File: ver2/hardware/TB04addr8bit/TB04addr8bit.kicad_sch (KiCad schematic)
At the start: 15 parts, among them J1 USB_C_Receptacle_PowerOnly_6P, SW1 SW_SPDT, U1 74AHC04, U2 74AHC04, U3 74LS157, U4 74HC138, U5 74HC00

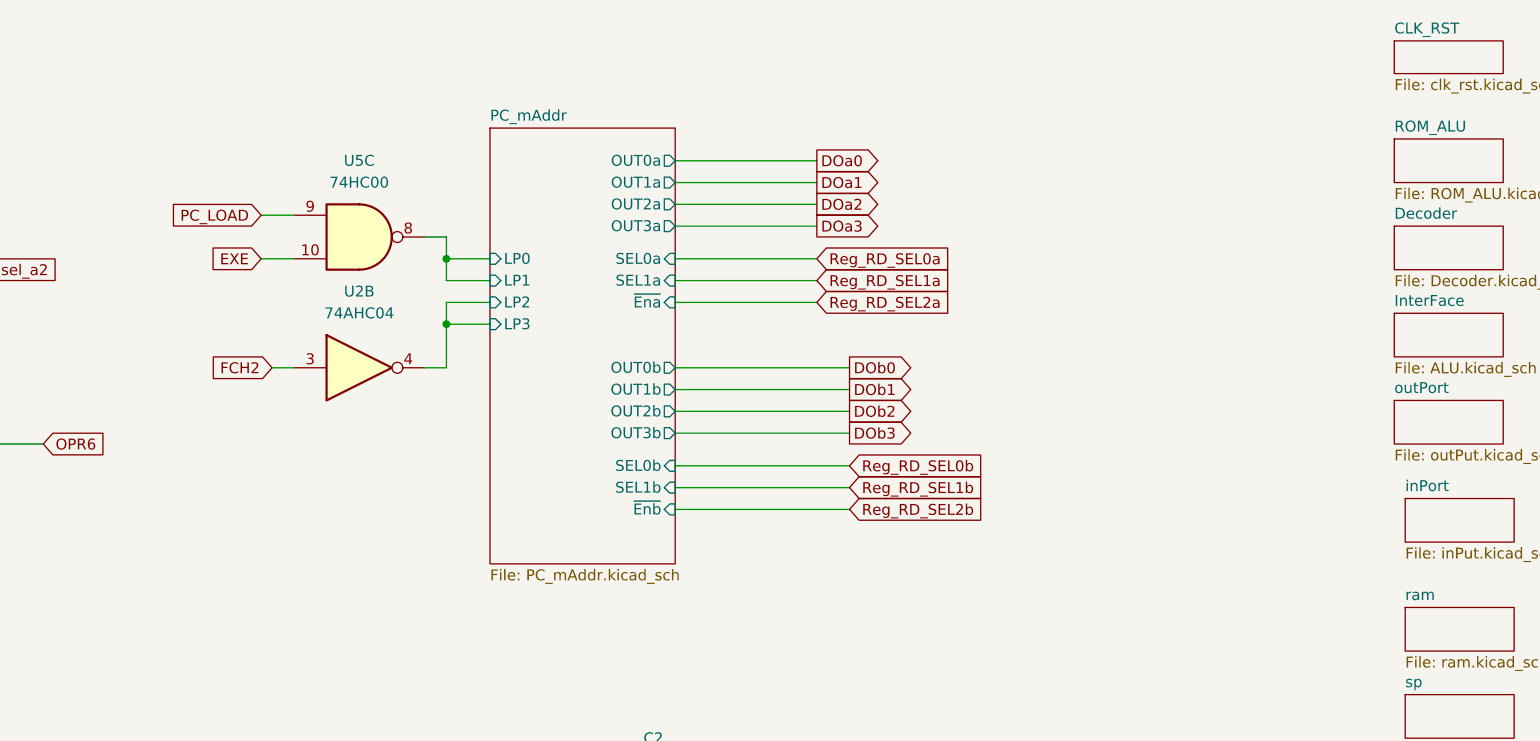
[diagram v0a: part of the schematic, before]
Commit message: ver2: 命令ラッチを1相ずらし、アドレスMUXを完成、I/Oと周辺ICを配置
- 命令ラッチの取り込みエッジを1相ずらし(U20 Cp=FCH1→FCH2 /
  U26 Cp=FCH2→DCR)。EXE中はアドレスバスがmAddrになるため、
  従来はEXE→FCH1の境目でROMのアクセスが間に合わなかった
- /OE_ROM のゲート入力を ~WE から ~WR へ付け替え
  (レジスタ書込許可ではなくメモリ書込で判定するのが正)
- PCの161出力をアドレスバスから切り離し、244経由に変更
  U42(PC)/U43(mAddr)/U44(SP)の入出力を結線し A0-A7 を駆動
  U44は 11110+SP[2:0] で 0xF0-0xF7 を生成。IN/OUT用の244は廃止
- PCのカウントイネーブルを 74LS32 の空きゲートで FCH1|FCH2 として生成
- PC_mAddr シートを PC へ改称し、分岐ロード用の 8bit 2:1 MUX
  (74LS157×2, U14/U15)を新設。出力 PC0-7 を161のD入力へ
  PCカウンタ(IC9/IC10)は addrMUX シートへ移動
- 6116 の /CS にゲートを追加(P2 & !P5)、D4-D7 にラベルを付与
- Yドライバ(74HC244×2, U16/U17)、inPort の 74LS253×2、
  outPort の 74HC273+LED4個 を配置(結線は未)
- ルートから未参照だった ROM_ALU_Decoder / interFace / RS02 を削除

未了: 共通8bitデータバス、オペランド源MUX(SEL_A/SEL_B/SEL_IMM/SEL_Y)、
I/Oポートの結線。PC_mAddr.kicad_sch は PC.kicad_sch と同一内容の
残骸として残っている

Co-Authored-By: Claude Opus 5 <noreply@anthropic.com>
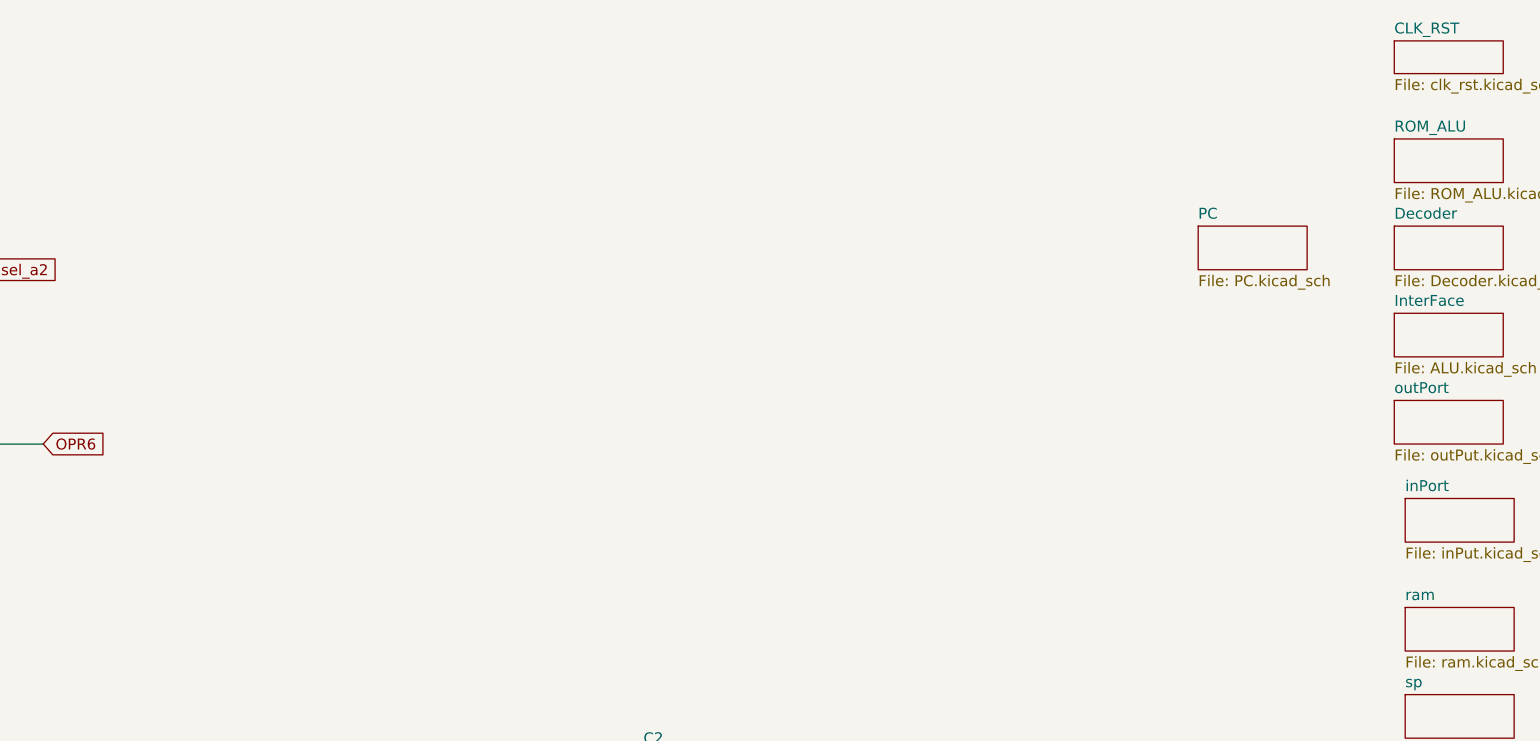
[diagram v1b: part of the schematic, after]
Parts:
- removed unit 2 of U2
- removed U5: 74HC00, symbol 74xx:74HC00
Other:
- sheet PC_mAddr renamed PC
- sheet PC: file PC_mAddr.kicad_sch -> PC.kicad_sch
- sheet PC ports: added none; removed LP0, LP1, LP2, LP3, OUT0a, OUT0b, OUT1a, OUT1b, OUT2a, OUT2b, OUT3a, OUT3b, SEL0a, SEL0b, SEL1a, SEL1b, ~{Ena}, ~{Enb}

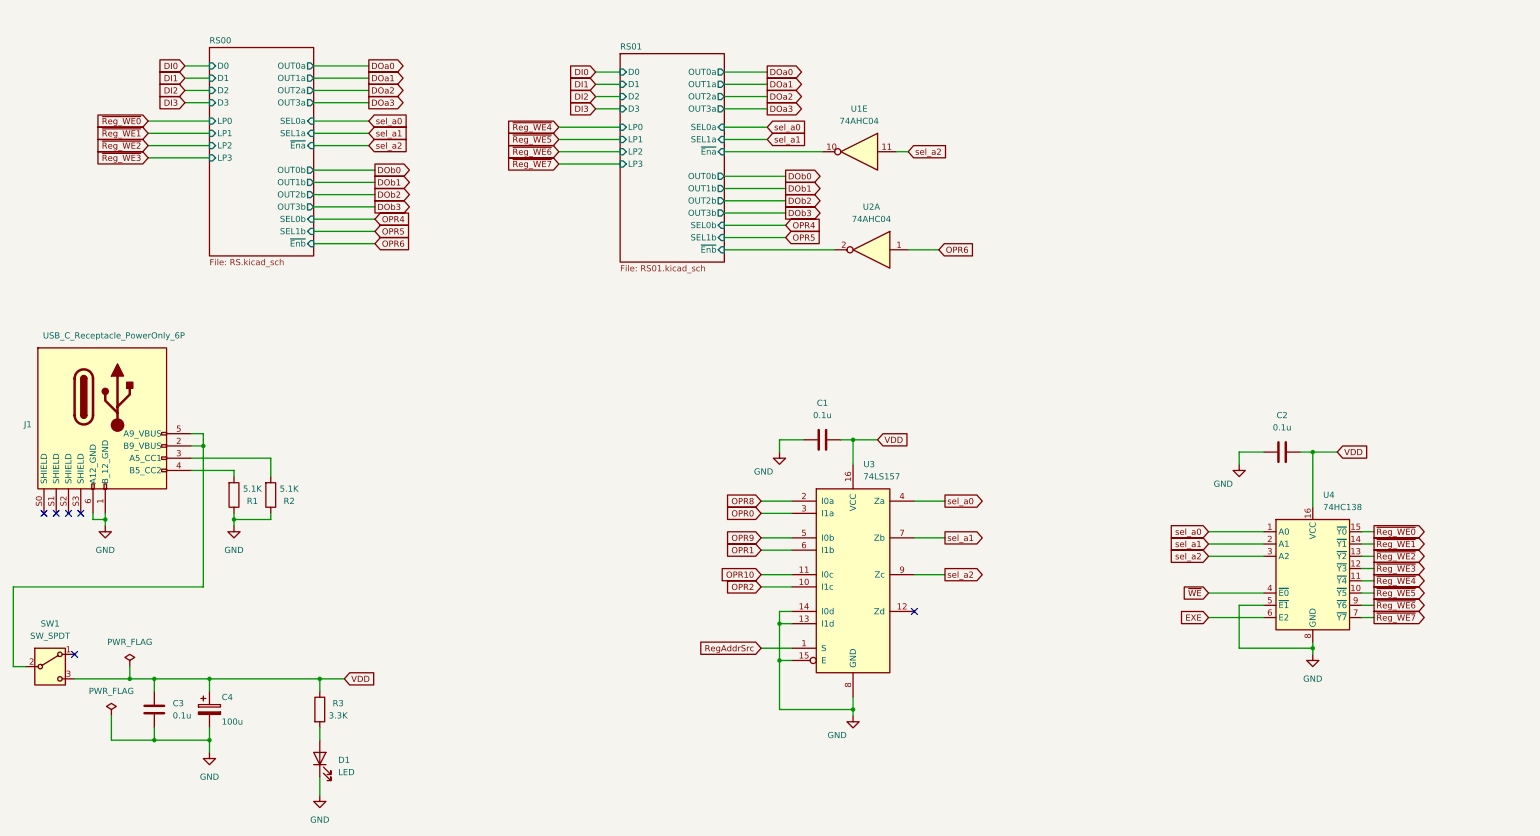
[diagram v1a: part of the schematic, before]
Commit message: ver2: 要修正5件を修正し共通データバス・オペランド源MUX・I/Oを結線
- 6116の/CS極性を修正し、スタック域を含むRAM_STK_SEL(0xC0-0xF7)に統一
- ALU出力をDI0-3へ直結、U21はYドライバ源として残す(LD/POP/RET対策)
- 共通8bitデータバスMD0-7を新設(ROM/RAM/Yドライバ/IN244が排他駆動)
- aポートMUX(74LS253x2)・IN用244・Yドライバ制御ゲートを追加
- IN実行時のROM競合を/OE_ROMに~OE_iAddrを足して回避
- 4bit書込時にMD4-7が浮くのをU17 bank2で0駆動
- 74LS157のEをGND固定、孤立したPC_mAddrシートを削除

Co-Authored-By: Claude Opus 5 <noreply@anthropic.com>
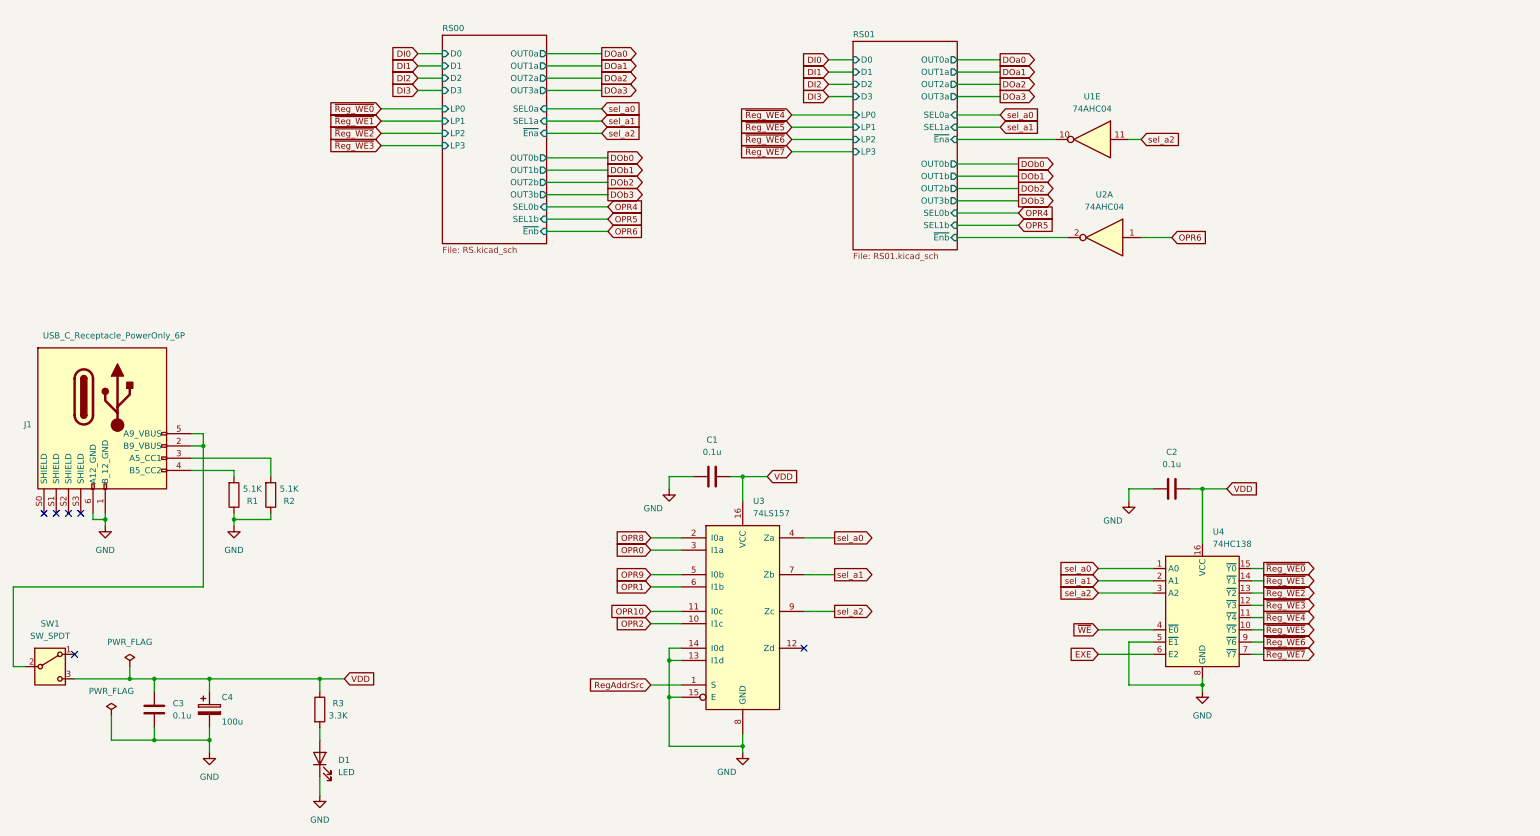
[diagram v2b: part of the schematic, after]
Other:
- moved on the sheet: C1, C2, U1E, U2A, U3, U4

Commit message: ver2: ゲートICをgatesシートへ集約しアノテーションを掛け直し
- 分散していた8パッケージ(U1/U2/U5/U25/U35/U36/U37/U51)をgatesシートへ集約
- シートをまたぐ11本をグローバルラベル化(~P4/~P5/~OUT_SEL/~CS_RAM/
  ~OE_ROM/CLK_C/CLK_Z/PC_CNT_EN/~PC_PE/~Ena_RS01/~Enb_RS01)
- U40のP2入力がROM_SELに吸着していたのを修正(RAM_SELが逆条件だった)
- !P5の重複インバータを解消、未使用ゲート入力7本をGNDへ
- ALU入力MUXをinPut→PC、PCカウンタをaddrMUX→PCへ移動
- 全体を再アノテーション(シート順採番)。旧→新の対応は電気的変化なしを確認

Co-Authored-By: Claude Opus 5 <noreply@anthropic.com>
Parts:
- removed U1, U2: 74AHC04, symbol 74xx:74AHC04
- renumbered C1 to C101, C2 to C102, C3 to C103, C4 to C104, D1 to D101, J1 to J101, R1 to R101, R2 to R102, R3 to R103, SW1 to SW101, U3 to U101, U4 to U102
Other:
- sheet PC renamed PC_aluMux (4 ページ)
- added sheet gates (gates.kicad_sch)
